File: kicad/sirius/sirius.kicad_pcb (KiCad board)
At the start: 4 copper layers, 42.1 x 65.5 mm, 60 parts, among them J1 IPEX_MHF1, J2 Power In, J3 Screw_Terminal, Q1 Q_PMOS_GSD, Q2 Q_NMOS_GSD, Q3 Q_NMOS_GSD, U1 Power_Connector, U2 AP63301WU-7, U3 XCVR_RFM95W-915S2, U4 LC29H (DA), U5 Pi Zero 2W

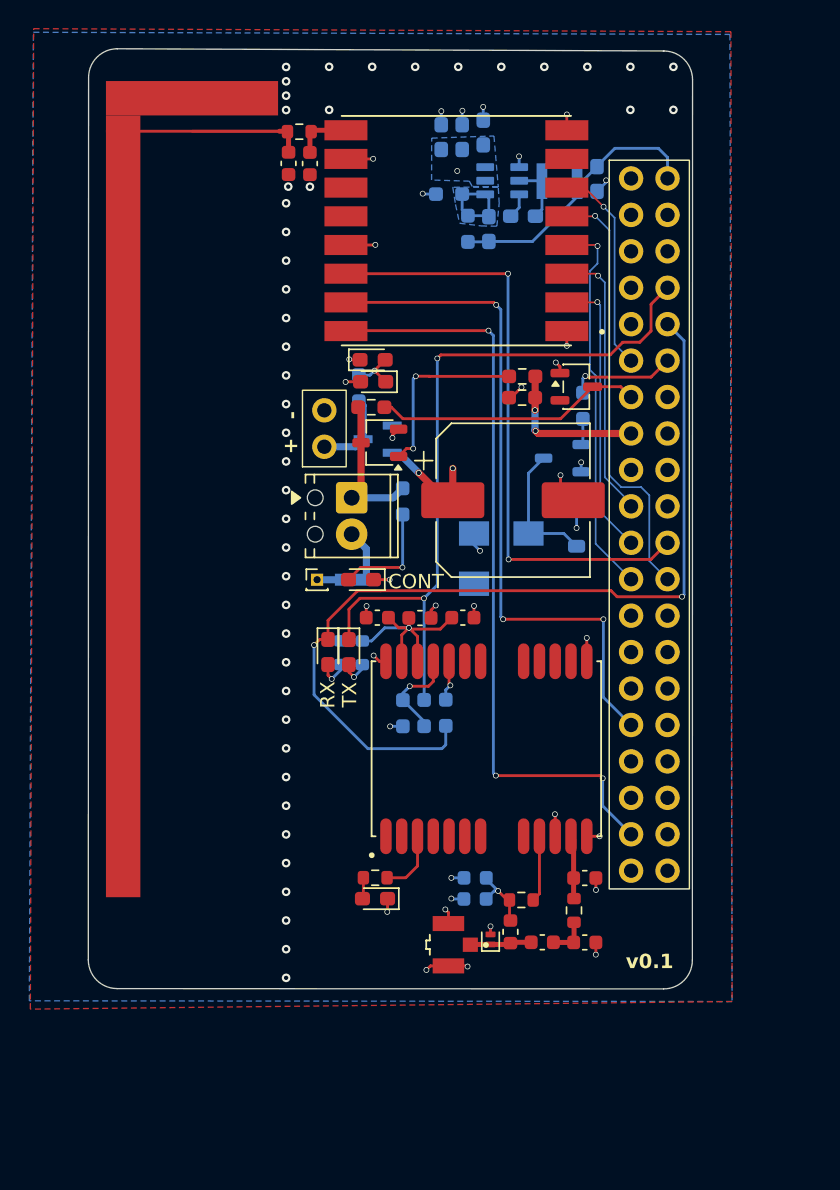
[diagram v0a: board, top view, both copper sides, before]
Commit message: Pass DRC, fix IFA net tie, restructure sirius and sopdet
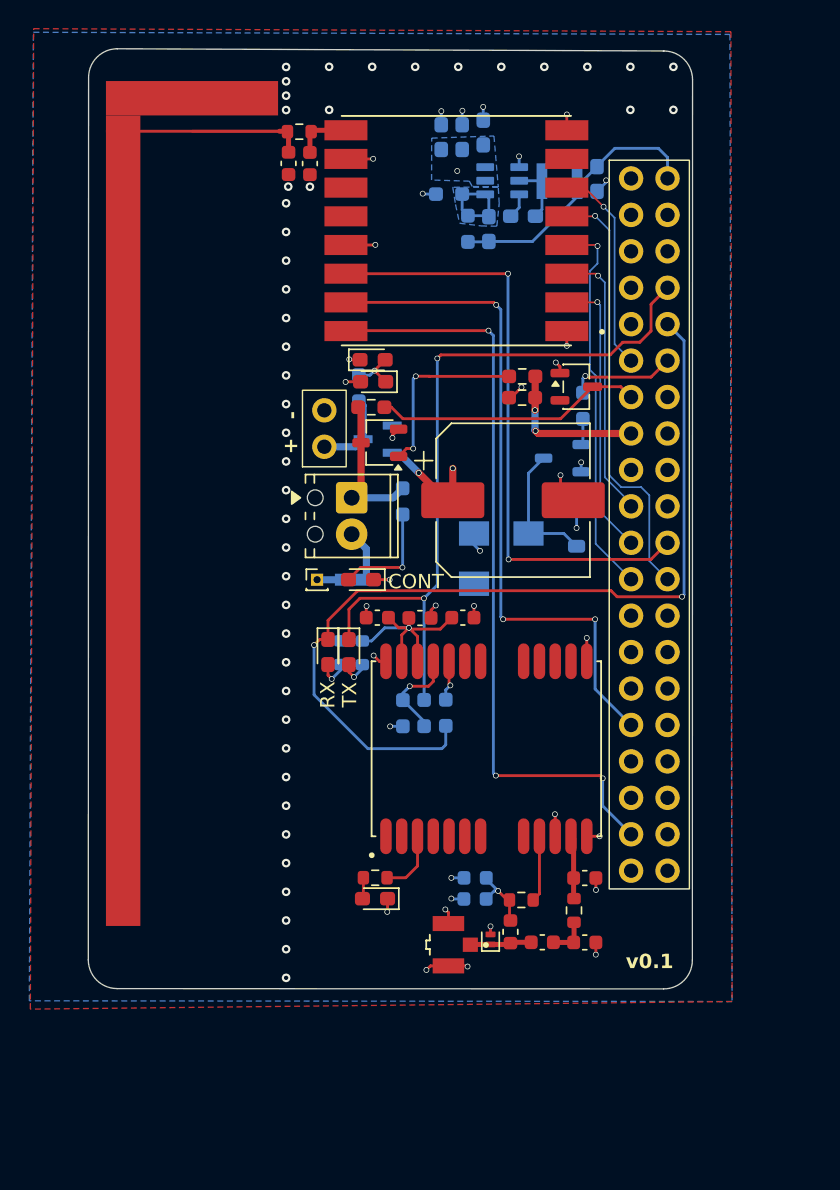
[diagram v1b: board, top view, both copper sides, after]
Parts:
- U3: value XCVR_RFM95W-915S2 -> RFM95W-915S2

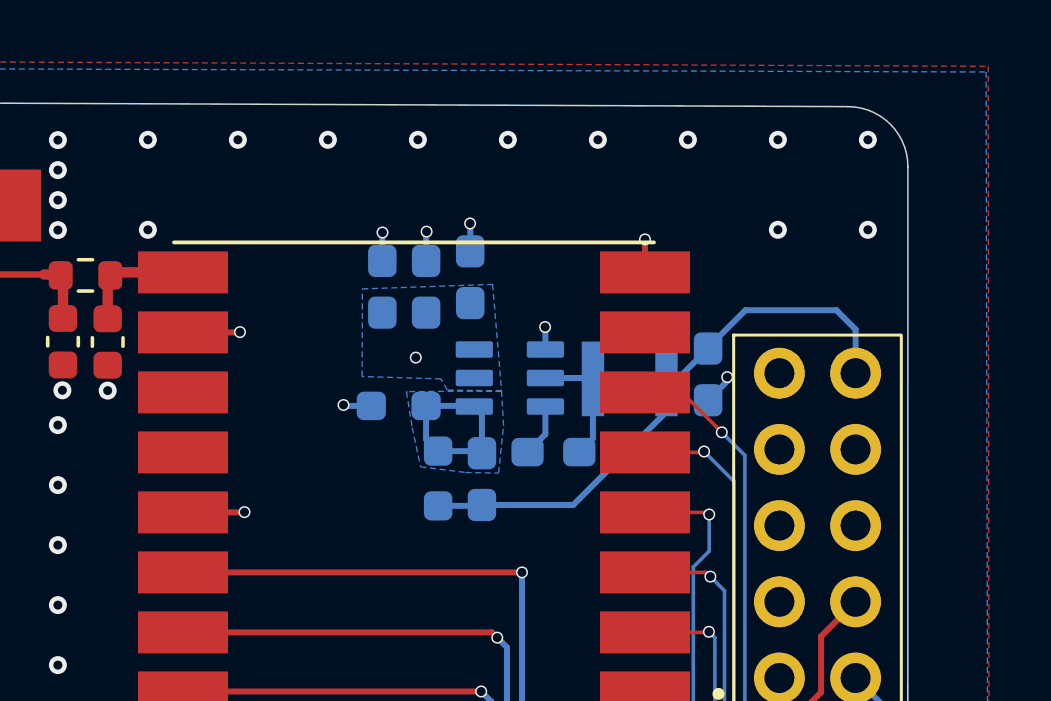
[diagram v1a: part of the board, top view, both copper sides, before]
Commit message: Finish routing Sopdet
Logo still pending
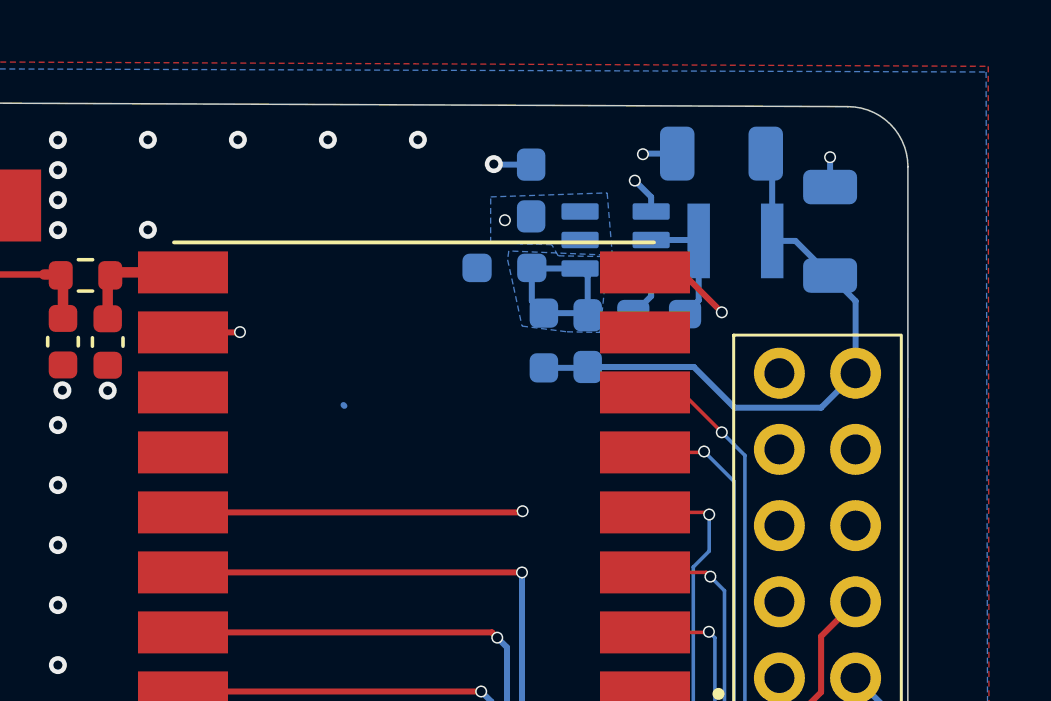
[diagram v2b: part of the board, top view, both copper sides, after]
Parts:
- removed the C1 at (139.1, 72.5)
- removed the C3 at (137.7, 72.5)
- added C7: 22u, Capacitor_SMD:C_1206_3216Metric, B.Cu at (149.0, 68.0)
- C6: renamed from C8; value 44u -> 22u; footprint Capacitor_SMD:C_0603_1608Metric_Pad1.08x0.95mm_HandSolder -> Capacitor_SMD:C_1206_3216Metric
- moved C6 6.27 mm to (152.6, 70.6), turned to 90 degrees
- moved C5 5.80 mm to (144.5, 74.3)
- moved R3 5.80 mm to (141.7, 71.8)
- moved C4 5.80 mm to (146.9, 73.4)
- moved L1 5.80 mm to (149.4, 70.9)
- moved R2 5.80 mm to (143.1, 74.2)
- moved U2 5.80 mm to (145.4, 70.9)
- moved C1 3.53 mm to (142.6, 69.2)
- renumbered C4 to C1, C11 to C10, C12 to C11, C13 to C12, C14 to C13, C15 to C14, C16 to C15, C17 to C16, C5 to C3, C6 to C4, C7 to C5, C9 to C8, C10 to C9, R3 to R2, R4 to R3, R2 to R4
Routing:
- net +3V3: track 90.5 -> 84.6 mm
- net VCC: track 28.7 -> 34.5 mm
- net +5V: track 21.5 -> 23.0 mm
- net GND: track 35.9 -> 37.0 mm, vias 80 -> 71

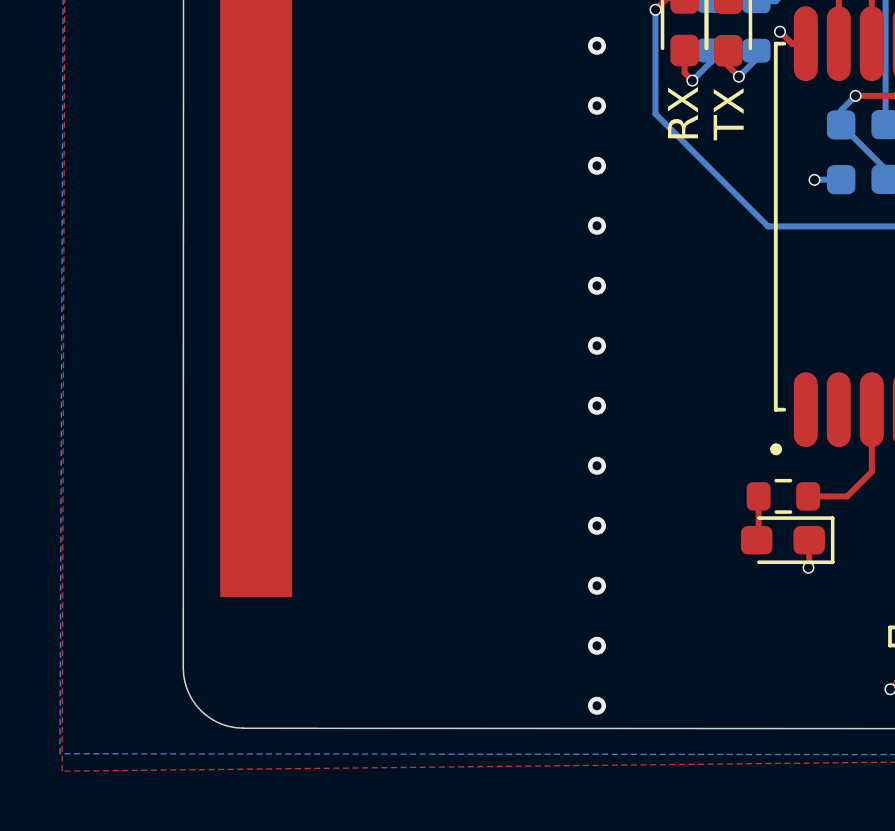
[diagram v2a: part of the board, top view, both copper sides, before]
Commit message: Finish Sopdet routing
Also add logos for Sirius and Sopdet
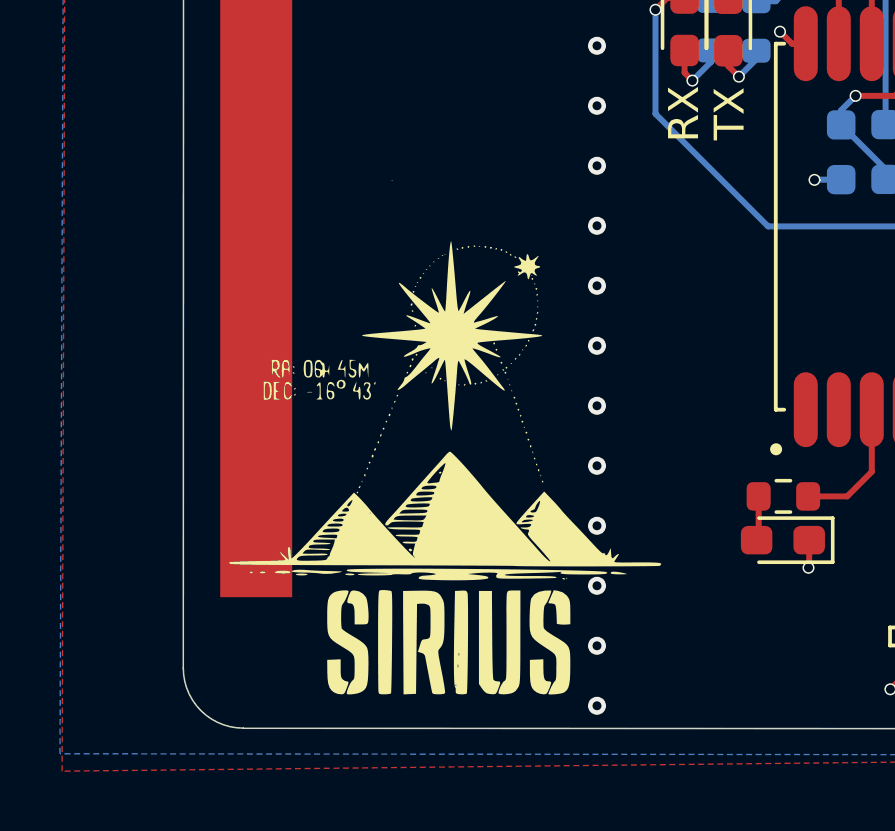
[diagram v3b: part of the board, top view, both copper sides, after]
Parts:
- added G***: LOGO, sirius:sirius_logo, F.Cu at (121.9, 121.6)

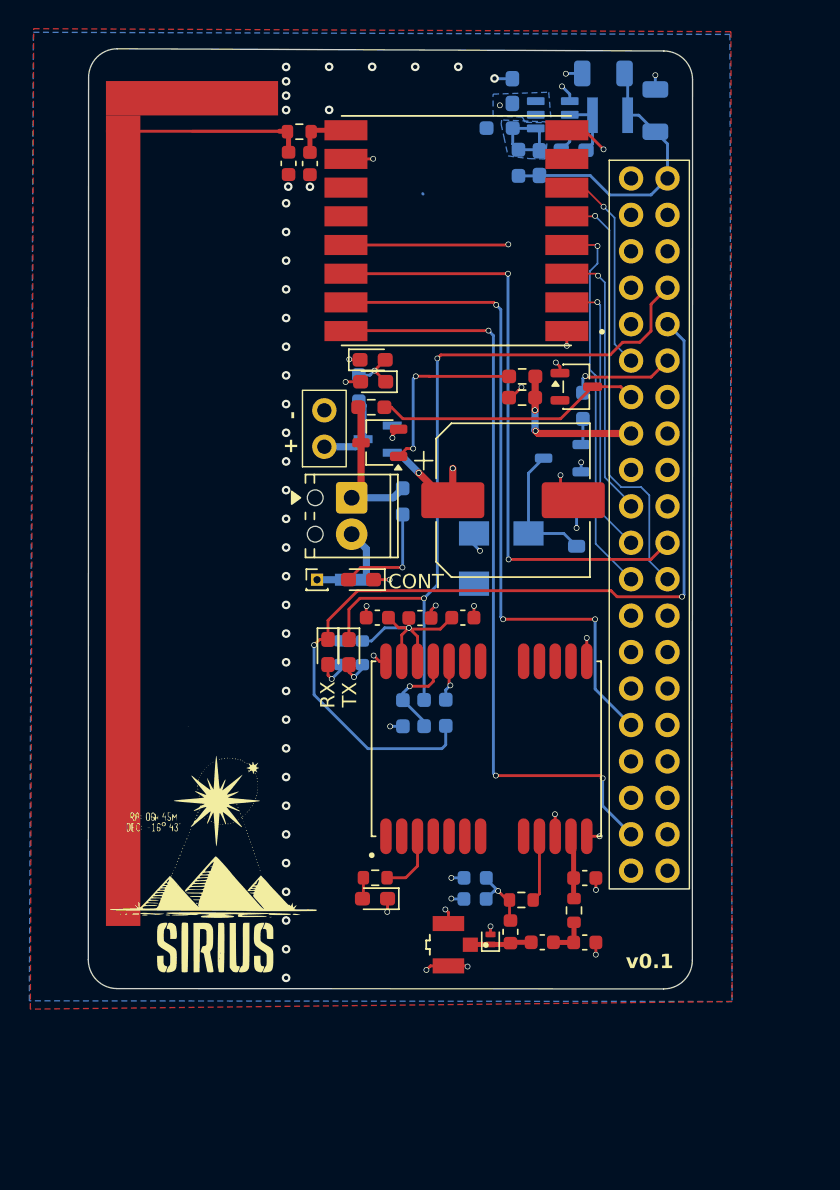
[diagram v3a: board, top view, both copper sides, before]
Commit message: Replace footprint of u.fl connector & screw terminal
Redesign board to accomodate larger footprint, make Sopdet a little smaller to qualify for $2 jlcpcb price, assign Digikey PN to all components, add a script which combines the BOM's of both boards so Digikey can more accurately detect cost savings
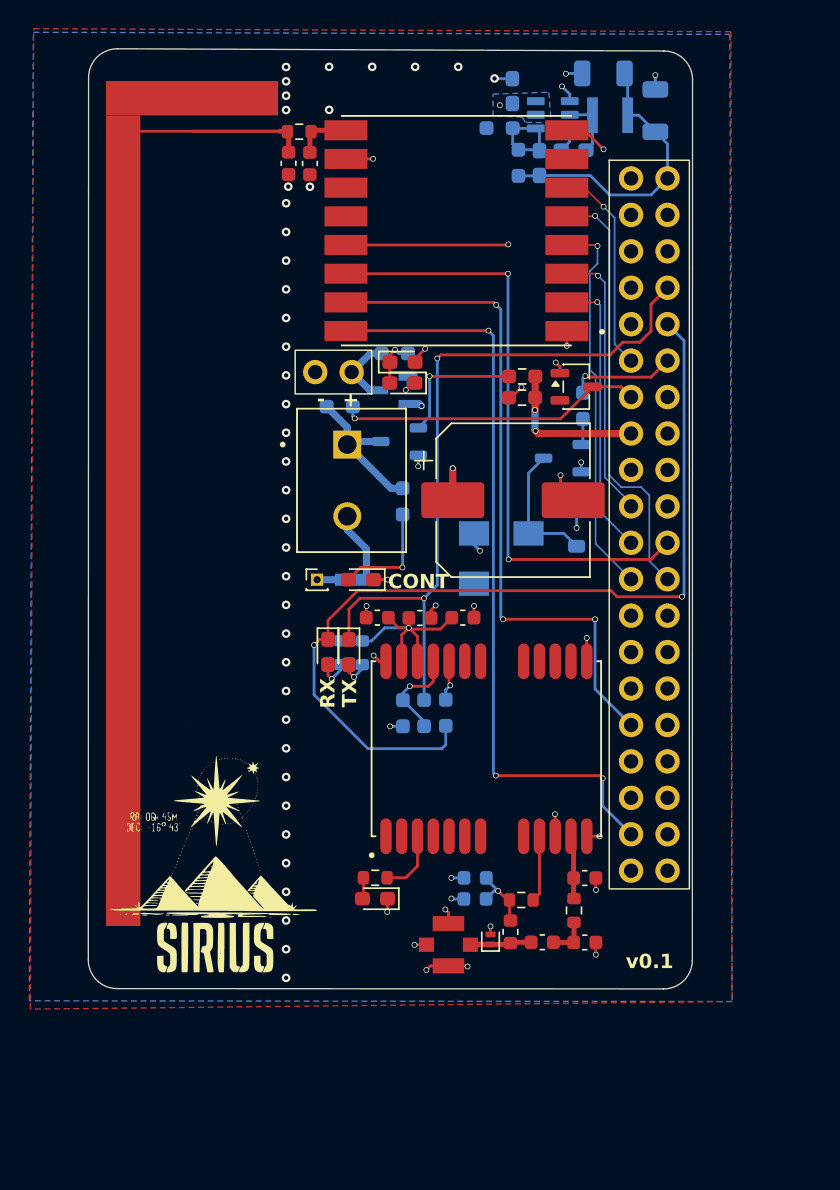
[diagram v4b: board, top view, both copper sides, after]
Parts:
- J1: footprint sirius:ipex_mhf1 -> sirius:TE_CONMHF1-SMD-T
- J3: footprint TerminalBlock_Phoenix:TerminalBlock_Phoenix_MPT-0,5-2-2.54_1x02_P2.54mm_Horizontal -> sirius:CUI_TB002-500-02BE
- Q2, R9: moved to B.Cu
- moved U1 3.98 mm to (130.2, 88.8), turned to 180 degrees
- moved J3 3.72 mm to (131.1, 93.9)
- moved Q1 3.58 mm to (134.3, 90.1)
- moved R4 3.49 mm to (134.4, 87.5), turned to 0 degrees
- moved D2 2.62 mm to (135.0, 89.6), turned to 180 degrees
- moved D1 2.46 mm to (135.0, 88.1), turned to 0 degrees
- moved R9 2.20 mm to (130.6, 91.2)
- moved Q2 1.38 mm to (134.8, 93.7)
- turned J1 to -90 degrees
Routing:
- net Net-(Q2-G): track 12.9 -> 9.47 mm, vias 2 -> 1
- net /CONTINUITY_SENSE: track 18.8 -> 21.4 mm, vias 0 -> 1
- net VCC: track 34.5 -> 32.1 mm
- net /PYRO_POSITIVE: track 3.60 -> 4.98 mm
- net /RESET: track 14.6 -> 13.4 mm
- net GND: track 37.0 -> 35.9 mm, vias 71 -> 72
- net Net-(D8-A): track 2.54 -> 1.83 mm
- net +BATT: track 5.68 -> 5.05 mm
- removed copper zone on B.Cu, net Net-(U2-FB)

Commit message: Add code for rocket and ground station
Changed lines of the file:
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@@
 	)
 	(gr_line
-		(start 113.07 129.815786)
+		(start 113.065796 129.815786)
 		(end 113.09 68.31)
 		(stroke
@@
 	)
 	(gr_arc
-		(start 115.07 131.815786)
-		(mid 113.655786 131.23)
-		(end 113.07 129.815786)
+		(start 115.074214 131.82)
+		(mid 113.654299 131.234471)
+		(end 113.065796 129.815786)
 		(stroke
 			(width 0.05)
